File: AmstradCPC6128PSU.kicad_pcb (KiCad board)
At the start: 2 copper layers, 35.6 x 22.9 mm, 3 parts, among them J1 DC 5V, J2 Mini-DIN-6, J3 DC 12V

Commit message: getting there
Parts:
- added H1: MountingHole_Pad, MountingHole:MountingHole_2.2mm_M2_Pad_Via, F.Cu at (123.8, 102.2)
- added H2: MountingHole_Pad, MountingHole:MountingHole_2.2mm_M2_Pad_Via, F.Cu at (153.0, 102.2)
- added J4: Conn_01x04_Male, Connector_PinHeader_2.54mm:PinHeader_1x04_P2.54mm_Vertical, F.Cu at (137.2, 85.1)
- moved J3 10.8 mm to (142.2, 89.5)
- moved J1 10.5 mm to (144.8, 97.3), turned to 270 degrees
- moved J2 2.51 mm to (129.5, 92.7)
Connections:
- J1 pad 1: Net-(J1-Pad1) -> /+5V
- J1 pad 2: Net-(J1-Pad2) -> /GND
- J2 pad 1: Net-(J2-Pad1) -> /+12V
- J2 pad 2: Net-(J2-Pad2) -> /+12V
- J2 pad 3: Net-(J1-Pad1) -> /+5V
- J2 pad 4: Net-(J2-Pad4) -> /GND
- J2 pad 5: Net-(J2-Pad5) -> /+5V
- J2 pad 6: Net-(J1-Pad2) -> /GND
- J2 pad 7: (no net) -> /GND
- J3 pad 1: Net-(J2-Pad1) -> /+12V
- J3 pad 2: Net-(J2-Pad5) -> /GND
- J3 pad 3: (no net) -> /SW
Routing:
- net Net-(J1-Pad1): track 25.8 -> 0.00 mm
- net /+5V: track 0.00 -> 24.8 mm
- net /+12V: track 0.00 -> 23.8 mm
- net Net-(J1-Pad2): track 22.3 -> 0.00 mm
- net Net-(J2-Pad1): track 18.6 -> 0.00 mm
- net Net-(J2-Pad5): track 17.1 -> 0.00 mm
- net /SW: track 0.00 -> 9.24 mm
- added copper zone on B.Cu, net /GND
- added copper zone on F.Cu, net /GND
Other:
- outline, holes or cut-outs redrawn
- net class 5-12V 2A added: clearance 0.4, trace_width 0.8, via_dia 0.8, via_drill 0.4
- board text added: "+12V"
- board text added: "+5V"
- board text added: "GND"
- board text added: "SW"
- board text added: "faxmodem 2020"

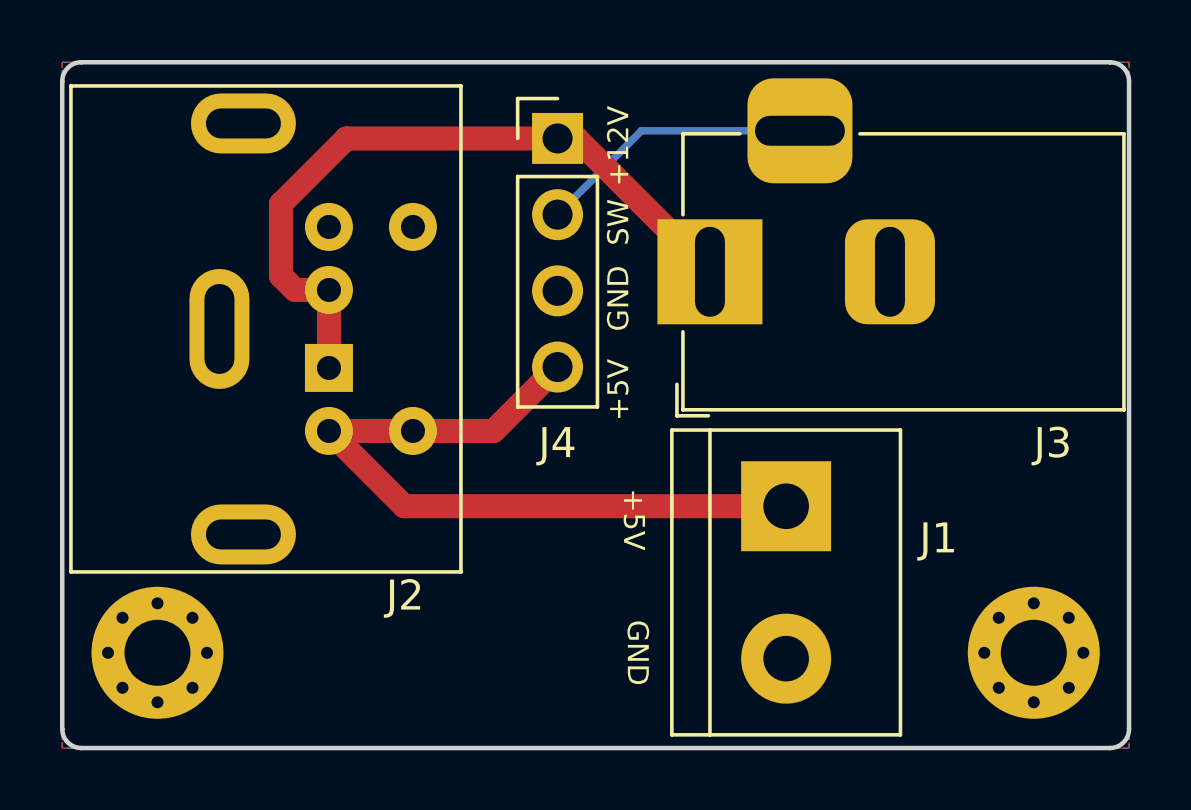
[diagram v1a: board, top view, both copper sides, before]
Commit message: Swap +5V and GND
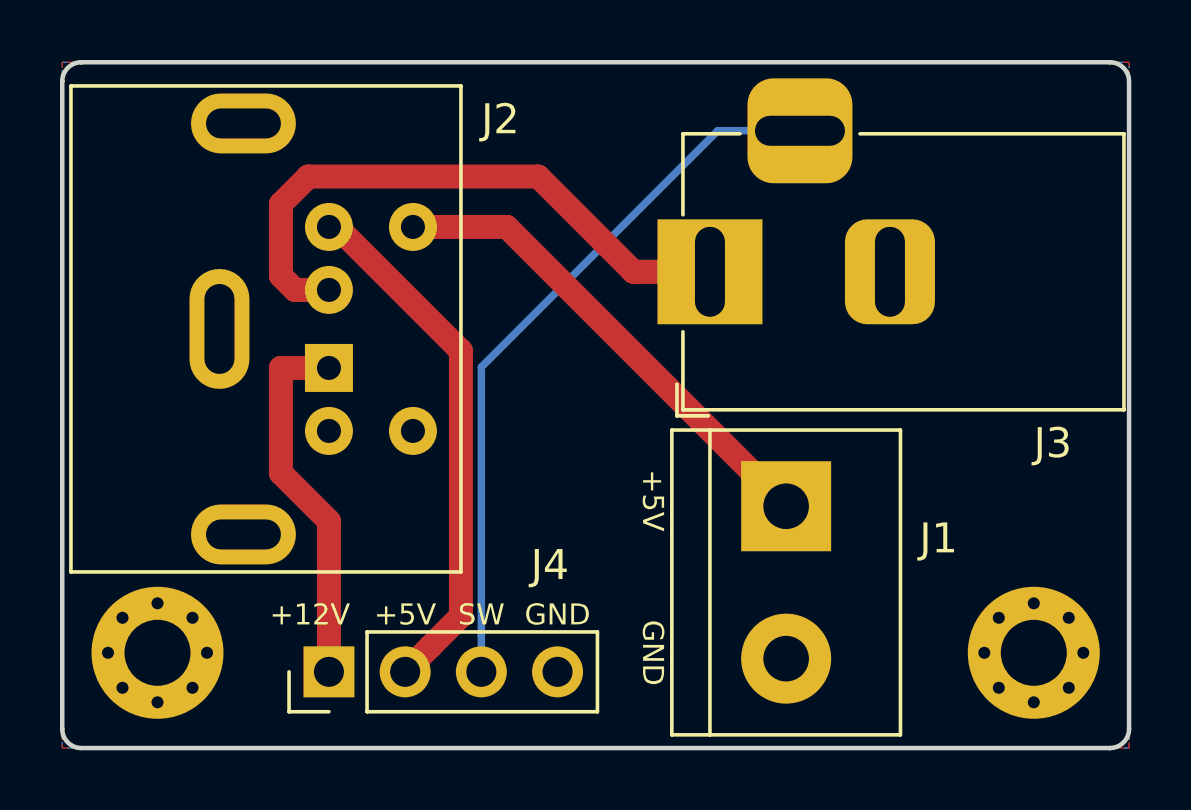
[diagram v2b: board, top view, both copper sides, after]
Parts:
- moved J4 19.3 mm to (129.5, 102.9), turned to 90 degrees
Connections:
- J2 pad 1: /+12V -> /+12Vb
- J2 pad 3: /+5V -> /GND
- J2 pad 4: /GND -> /+5Vb
- J2 pad 5: /+5V -> /GND
- J2 pad 6: /GND -> /+5V
- J4 pad 1: /+12V -> /+12Vb
- J4 pad 2: /SW -> /+5Vb
- J4 pad 3: /GND -> /SW
- J4 pad 4: /+5V -> /GND
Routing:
- net /+5Vb: track 0.00 -> 17.6 mm
- net /SW: track 9.24 -> 24.0 mm
- net /+12Vb: track 0.00 -> 12.4 mm
- net /+5V: track 24.8 -> 16.3 mm
- net /+12V: track 23.8 -> 20.2 mm

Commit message: Add gitignore
Use github provided gitignore
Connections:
- J3 pad 1: /+12V -> /GND
- J3 pad 2: /GND -> /+12V
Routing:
- net /+12V: track 20.2 -> 28.3 mm
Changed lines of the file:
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@@
     (thickness 1.6)
     (drawings 15)
-    (tracks 23)
+    (tracks 26)
     (zones 0)
     (modules 6)
@@
     (32 B.Adhes user hide)
     (33 F.Adhes user hide)
-    (34 B.Paste user hide)
-    (35 F.Paste user hide)
+    (34 B.Paste user)
+    (35 F.Paste user)
     (36 B.SilkS user)
     (37 F.SilkS user)
@@
     (fp_line (start 0 -4.5) (end -13.7 -4.5) (layer F.Fab) (width 0.1))
     (pad 1 thru_hole rect (at 0 0 180) (size 3.5 3.5) (drill oval 1 3) (layers *.Cu *.Mask)
+      (net 2 /GND))
+    (pad 2 thru_hole roundrect (at -6 0 180) (size 3 3.5) (drill oval 1 3) (layers *.Cu *.Mask) (roundrect_rratio 0.25)
       (net 3 /+12V))
-    (pad 2 thru_hole roundrect (at -6 0 180) (size 3 3.5) (drill oval 1 3) (layers *.Cu *.Mask) (roundrect_rratio 0.25)
-      (net 2 /GND))
     (pad 3 thru_hole roundrect (at -3 4.7 180) (size 3.5 3.5) (drill oval 3 1) (layers *.Cu *.Mask) (roundrect_rratio 0.25)
       (net 4 /SW))
@@
   (gr_line (start 156.21 104.775) (end 156.21 83.185) (layer Edge.Cuts) (width 0.15))
   (gr_line (start 121.285 105.41) (end 155.575 105.41) (layer Edge.Cuts) (width 0.15))
-  (segment (start 135.47 88.04) (end 144.78 97.35) (width 0.8) (layer F.Cu) (net 1))
-  (segment (start 132.34 88.04) (end 135.47 88.04) (width 0.8) (layer F.Cu) (net 1))
+  (segment (start 132.34 88.04) (end 142.24 97.155) (width 0.8) (layer F.Cu) (net 1))
+  (segment (start 142.435 97.35) (end 142.24 97.155) (width 0.8) (layer F.Cu) (net 1))
+  (segment (start 144.78 97.35) (end 142.435 97.35) (width 0.8) (layer F.Cu) (net 1))
+  (segment (start 127.939999 87.271999) (end 128.851998 86.36) (width 0.8) (layer F.Cu) (net 3))
   (segment (start 127.939999 89.671369) (end 127.939999 87.271999) (width 0.8) (layer F.Cu) (net 3))
   (segment (start 128.40863 90.14) (end 127.939999 89.671369) (width 0.8) (layer F.Cu) (net 3))
-  (segment (start 127.939999 87.271999) (end 128.851998 86.36) (width 0.8) (layer F.Cu) (net 3))
   (segment (start 129.54 90.14) (end 128.40863 90.14) (width 0.8) (layer F.Cu) (net 3))
-  (segment (start 139.69 89.535) (end 142.24 89.535) (width 0.8) (layer F.Cu) (net 3))
-  (segment (start 136.515 86.36) (end 139.69 89.535) (width 0.8) (layer F.Cu) (net 3))
-  (segment (start 128.851998 86.36) (end 136.515 86.36) (width 0.8) (layer F.Cu) (net 3))
+  (segment (start 146.779545 90.995455) (end 148.24 89.535) (width 0.8) (layer F.Cu) (net 3))
+  (segment (start 139.849999 92.085001) (end 145.689999 92.085001) (width 0.8) (layer F.Cu) (net 3))
+  (segment (start 134.124998 86.36) (end 139.849999 92.085001) (width 0.8) (layer F.Cu) (net 3))
+  (segment (start 145.689999 92.085001) (end 146.779545 90.995455) (width 0.8) (layer F.Cu) (net 3))
+  (segment (start 128.851998 86.36) (end 134.124998 86.36) (width 0.8) (layer F.Cu) (net 3))
   (segment (start 142.494998 84.835) (end 134.62 92.709998) (width 0.25) (layer B.Cu) (net 4))
   (segment (start 134.62 101.667919) (end 134.62 102.87) (width 0.25) (layer B.Cu) (net 4))
